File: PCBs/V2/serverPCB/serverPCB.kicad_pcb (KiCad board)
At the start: 2 copper layers, 53.3 x 66 mm, 8 parts, among them J2 Screw_Terminal_01x04, U4 TPSM84203

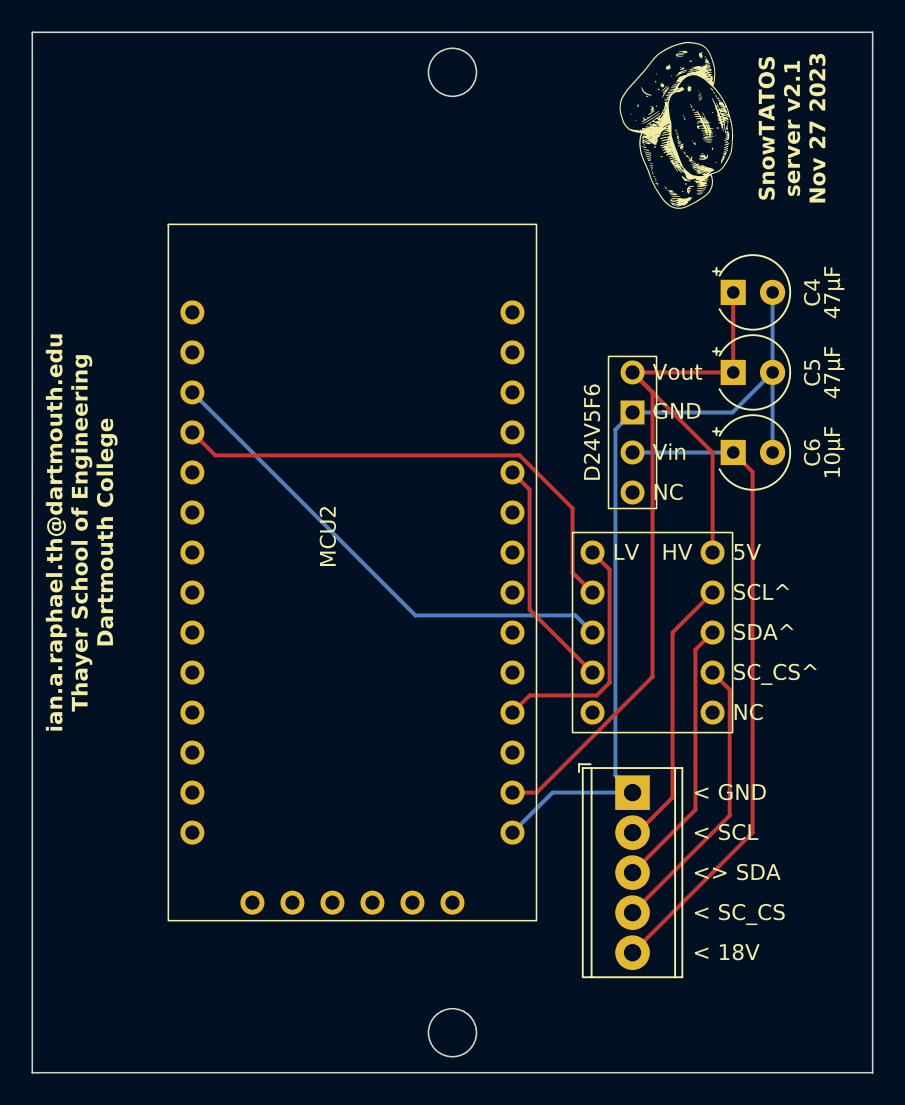
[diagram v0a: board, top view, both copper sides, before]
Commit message: fully updated but untested server/node code for new mini ultra boards
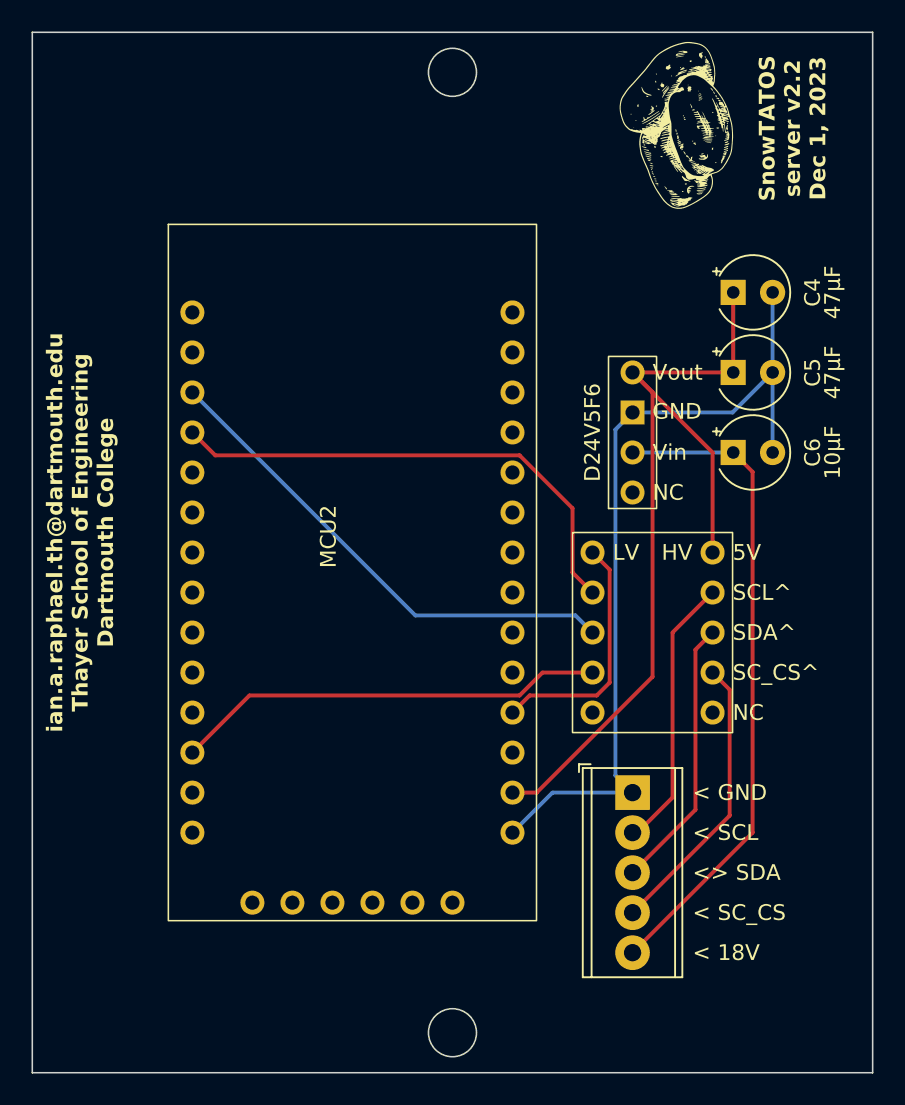
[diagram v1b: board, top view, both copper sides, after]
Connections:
- MCU2 pad 11: unconnected-(MCU2-D11-Pad11) -> /SC_CS
- MCU2 pad A2: Net-(MCU2-A2_D14) -> unconnected-(MCU2-A2_D14-PadA2)
- U3 pad 4: Net-(MCU2-A2_D14) -> /SC_CS
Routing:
- net /SC_CS: track 0.00 -> 27.5 mm
- net Net-(MCU2-A2_D14): track 14.8 -> 0.00 mm
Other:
- board text added: "SnowTATOS server v2.2 Dec 1, 2023"
- board text removed: "SnowTATOS server v2.1 Nov 27 2023"
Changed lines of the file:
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@@
   (net 20 "unconnected-(MCU2-RXD1-Pad9)")
   (net 21 "unconnected-(MCU2-LORA_DIO_0-Pad10)")
-  (net 22 "unconnected-(MCU2-D11-Pad11)")
+  (net 22 "/SC_CS")
   (net 23 "unconnected-(MCU2-LORA_CS-Pad12)")
   (net 24 "unconnected-(MCU2-D13_A1-Pad13)")
@@
   (net 26 "unconnected-(MCU2-D23-Pad23)")
   (net 27 "unconnected-(MCU2-D24-Pad24)")
-  (net 28 "Net-(MCU2-A2_D14)")
+  (net 28 "unconnected-(MCU2-A2_D14-PadA2)")
   (net 29 "unconnected-(MCU2-A3_D15-PadA3)")
   (net 30 "unconnected-(MCU2-A4_D16-PadA4)")
@@
       (net 21 "unconnected-(MCU2-LORA_DIO_0-Pad10)") (pinfunction "LORA_DIO_0") (pintype "bidirectional"))
     (pad "11" thru_hole circle (at -10.16 7.62) (size 1.524 1.524) (drill 0.9) (layers "*.Cu" "*.Mask")
-      (net 22 "unconnected-(MCU2-D11-Pad11)") (pinfunction "D11") (pintype "unspecified"))
+      (net 22 "/SC_CS") (pinfunction "D11") (pintype "unspecified"))
     (pad "12" thru_hole circle (at -10.16 10.16) (size 1.524 1.524) (drill 0.9) (layers "*.Cu" "*.Mask")
       (net 23 "unconnected-(MCU2-LORA_CS-Pad12)") (pinfunction "LORA_CS") (pintype "output"))
@@
       (net 8 "unconnected-(MCU2-D25-Pad25)") (pinfunction "D25") (pintype "bidirectional"))
     (pad "A2" thru_hole circle (at 10.16 -10.16) (size 1.524 1.524) (drill 0.9) (layers "*.Cu" "*.Mask")
-      (net 28 "Net-(MCU2-A2_D14)") (pinfunction "A2_D14") (pintype "bidirectional"))
+      (net 28 "unconnected-(MCU2-A2_D14-PadA2)") (pinfunction "A2_D14") (pintype "bidirectional"))
     (pad "A3" thru_hole circle (at 10.16 -12.7) (size 1.524 1.524) (drill 0.9) (layers "*.Cu" "*.Mask")
       (net 29 "unconnected-(MCU2-A3_D15-PadA3)") (pinfunction "A3_D15") (pintype "bidirectional"))
@@
       (net 7 "/SDA") (pinfunction "L2") (pintype "bidirectional"))
     (pad "4" thru_hole circle (at -3.81 2.54) (size 1.524 1.524) (drill 0.9) (layers "*.Cu" "*.Mask")
-      (net 28 "Net-(MCU2-A2_D14)") (pinfunction "L3") (pintype "bidirectional"))
+      (net 22 "/SC_CS") (pinfunction "L3") (pintype "bidirectional"))
     (pad "5" thru_hole circle (at -3.81 5.08) (size 1.524 1.524) (drill 0.9) (layers "*.Cu" "*.Mask")
       (net 9 "unconnected-(U3-L4-Pad5)") (pinfunction "L4") (pintype "bidirectional+no_connect"))
@@
     (effects (font (size 1 1) (thickness 0.15)) (justify left))
   )
-  (gr_text "SnowTATOS\nserver v2.1\nNov 27 2023" (at 162.56 64.516 90) (layer "F.SilkS")
+  (gr_text "SnowTATOS\nserver v2.2\nDec 1, 2023" (at 162.56 64.516 90) (layer "F.SilkS")
     (effects (font (size 1 1) (thickness 0.2) bold))
   )
@@
   (segment (start 158.79 74.93) (end 158.79 80.01) (width 0.25) (layer "F.Cu") (net 10))
   (segment (start 152.4 80.01) (end 157.48 85.09) (width 0.25) (layer "F.Cu") (net 10))
-  (segment (start 145.867 87.447) (end 145.867 95.067) (width 0.25) (layer "F.Cu") (net 28))
-  (segment (start 145.867 95.067) (end 149.86 99.06) (width 0.25) (layer "F.Cu") (net 28))
-  (segment (start 144.78 86.36) (end 145.867 87.447) (width 0.25) (layer "F.Cu") (net 28))
+  (segment (start 128.086823 100.513177) (end 124.46 104.14) (width 0.25) (layer "F.Cu") (net 22))
+  (segment (start 145.230427 100.513177) (end 128.086823 100.513177) (width 0.25) (layer "F.Cu") (net 22))
+  (segment (start 146.683604 99.06) (end 145.230427 100.513177) (width 0.25) (layer "F.Cu") (net 22))
+  (segment (start 149.86 99.06) (end 146.683604 99.06) (width 0.25) (layer "F.Cu") (net 22))
   (segment (start 160.02 109.22) (end 160.02 86.32) (width 0.25) (layer "F.Cu") (net 39))
   (segment (start 160.02 86.32) (end 158.79 85.09) (width 0.25) (layer "F.Cu") (net 39))

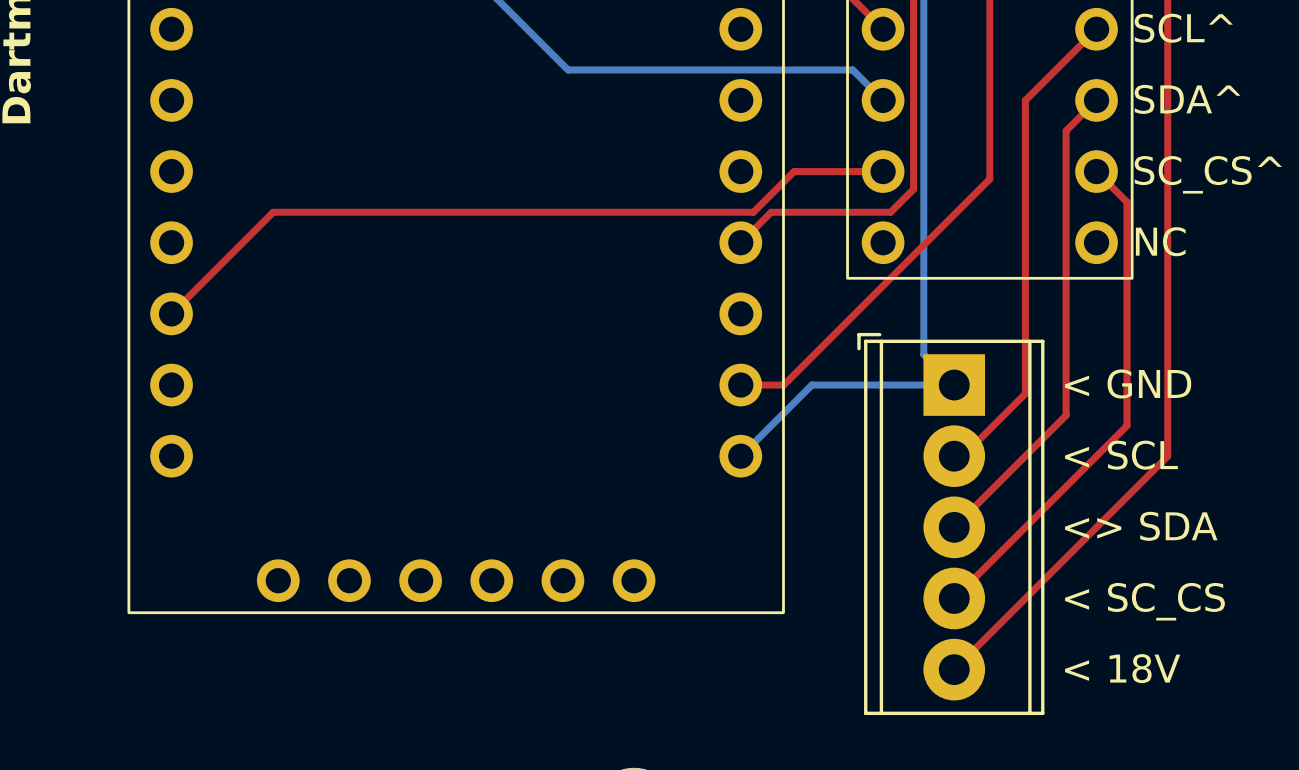
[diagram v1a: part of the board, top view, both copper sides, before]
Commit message: successful server integration into barebones simb program and full simb suite with dummy buffer
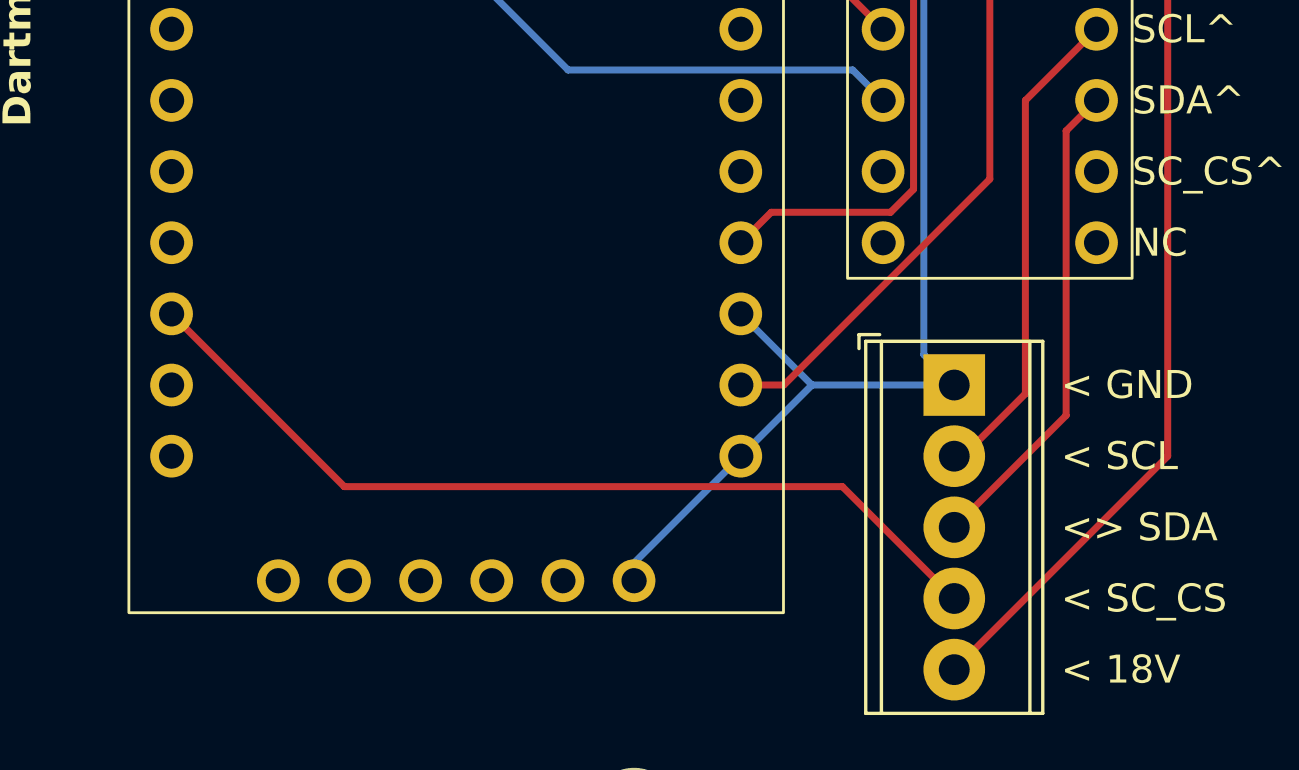
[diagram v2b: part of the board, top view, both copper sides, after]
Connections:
- J2 pad 4: Net-(J2-Pin_4) -> /SC_CS
- U3 pad 4: /SC_CS -> unconnected-(U3-L3-Pad4)
- U3 pad 9: Net-(J2-Pin_4) -> unconnected-(U3-H3-Pad9)
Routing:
- net Net-(J2-Pin_4): track 18.2 -> 0.00 mm
- net /GND: track 53.8 -> 63.4 mm
- net /SC_CS: track 27.5 -> 32.1 mm
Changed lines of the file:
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@@
   (net 2 "Net-(J2-Pin_2)")
   (net 3 "Net-(J2-Pin_3)")
-  (net 4 "Net-(J2-Pin_4)")
+  (net 4 "unconnected-(U3-L3-Pad4)")
   (net 5 "/3v3")
   (net 6 "/SCL")
@@
   (net 38 "unconnected-(MCU2-PadVIN)")
   (net 39 "Net-(J2-Pin_5)")
+  (net 40 "unconnected-(U3-H3-Pad9)")
   (footprint "Capacitor_THT:CP_Radial_Tantal_D4.5mm_P2.50mm" (layer "F.Cu")
     (at 158.79 85.09)
@@
       (net 3 "Net-(J2-Pin_3)") (pinfunction "Pin_3") (pintype "passive"))
     (pad "4" thru_hole circle (at 7.62 0 270) (size 2.2 2.2) (drill 1.1) (layers "*.Cu" "*.Mask")
-      (net 4 "Net-(J2-Pin_4)") (pinfunction "Pin_4") (pintype "passive"))
+      (net 22 "/SC_CS") (pinfunction "Pin_4") (pintype "passive"))
     (pad "5" thru_hole circle (at 10.16 0 270) (size 2.2 2.2) (drill 1.1) (layers "*.Cu" "*.Mask")
       (net 39 "Net-(J2-Pin_5)") (pinfunction "Pin_5") (pintype "passive"))
@@
       (net 7 "/SDA") (pinfunction "L2") (pintype "bidirectional"))
     (pad "4" thru_hole circle (at -3.81 2.54) (size 1.524 1.524) (drill 0.9) (layers "*.Cu" "*.Mask")
-      (net 22 "/SC_CS") (pinfunction "L3") (pintype "bidirectional"))
+      (net 4 "unconnected-(U3-L3-Pad4)") (pinfunction "L3") (pintype "bidirectional"))
     (pad "5" thru_hole circle (at -3.81 5.08) (size 1.524 1.524) (drill 0.9) (layers "*.Cu" "*.Mask")
       (net 9 "unconnected-(U3-L4-Pad5)") (pinfunction "L4") (pintype "bidirectional+no_connect"))
@@
       (net 3 "Net-(J2-Pin_3)") (pinfunction "H2") (pintype "bidirectional"))
     (pad "9" thru_hole circle (at 3.81 2.54) (size 1.524 1.524) (drill 0.9) (layers "*.Cu" "*.Mask")
-      (net 4 "Net-(J2-Pin_4)") (pinfunction "H3") (pintype "bidirectional"))
+      (net 40 "unconnected-(U3-H3-Pad9)") (pinfunction "H3") (pintype "bidirectional"))
     (pad "10" thru_hole circle (at 3.81 5.08) (size 1.524 1.524) (drill 0.9) (layers "*.Cu" "*.Mask")
       (net 11 "unconnected-(U3-H4-Pad10)") (pinfunction "H4") (pintype "bidirectional+no_connect"))
@@
   (segment (start 161.29 80.01) (end 158.75 82.55) (width 0.25) (layer "B.Cu") (net 1))
   (segment (start 152.4 106.68) (end 147.32 106.68) (width 0.25) (layer "B.Cu") (net 1))
+  (segment (start 144.78 109.22) (end 140.97 113.03) (width 0.25) (layer "B.Cu") (net 1))
   (segment (start 158.75 82.55) (end 152.4 82.55) (width 0.25) (layer "B.Cu") (net 1))
   (segment (start 161.29 74.93) (end 161.29 85.09) (width 0.25) (layer "B.Cu") (net 1))
+  (segment (start 140.97 113.03) (end 140.97 113.665) (width 0.25) (layer "B.Cu") (net 1))
   (segment (start 151.313 83.637) (end 151.313 105.593) (width 0.25) (layer "B.Cu") (net 1))
   (segment (start 152.4 82.55) (end 151.313 83.637) (width 0.25) (layer "B.Cu") (net 1))
+  (segment (start 147.32 106.68) (end 144.78 104.14) (width 0.25) (layer "B.Cu") (net 1))
   (segment (start 151.313 105.593) (end 152.4 106.68) (width 0.25) (layer "B.Cu") (net 1))
   (segment (start 152.71 109.22) (end 154.94 106.99) (width 0.25) (layer "F.Cu") (net 2))
@@
   (segment (start 156.393 107.767) (end 156.393 97.607) (width 0.25) (layer "F.Cu") (net 3))
   (segment (start 156.393 97.607) (end 157.48 96.52) (width 0.25) (layer "F.Cu") (net 3))
-  (segment (start 152.4 114.3) (end 158.567 108.133) (width 0.25) (layer "F.Cu") (net 4))
-  (segment (start 158.567 108.133) (end 158.567 100.147) (width 0.25) (layer "F.Cu") (net 4))
-  (segment (start 158.567 100.147) (end 157.48 99.06) (width 0.25) (layer "F.Cu") (net 4))
   (segment (start 150.947 99.693251) (end 150.127251 100.513) (width 0.25) (layer "F.Cu") (net 5))
   (segment (start 145.867 100.513) (end 144.78 101.6) (width 0.25) (layer "F.Cu") (net 5))
@@
   (segment (start 158.79 74.93) (end 158.79 80.01) (width 0.25) (layer "F.Cu") (net 10))
   (segment (start 152.4 80.01) (end 157.48 85.09) (width 0.25) (layer "F.Cu") (net 10))
-  (segment (start 128.086823 100.513177) (end 124.46 104.14) (width 0.25) (layer "F.Cu") (net 22))
-  (segment (start 145.230427 100.513177) (end 128.086823 100.513177) (width 0.25) (layer "F.Cu") (net 22))
-  (segment (start 146.683604 99.06) (end 145.230427 100.513177) (width 0.25) (layer "F.Cu") (net 22))
-  (segment (start 149.86 99.06) (end 146.683604 99.06) (width 0.25) (layer "F.Cu") (net 22))
+  (segment (start 124.46 104.14) (end 130.627 110.307) (width 0.25) (layer "F.Cu") (net 22))
+  (segment (start 148.407 110.307) (end 152.4 114.3) (width 0.25) (layer "F.Cu") (net 22))
+  (segment (start 130.627 110.307) (end 148.407 110.307) (width 0.25) (layer "F.Cu") (net 22))
   (segment (start 160.02 109.22) (end 160.02 86.32) (width 0.25) (layer "F.Cu") (net 39))
   (segment (start 160.02 86.32) (end 158.79 85.09) (width 0.25) (layer "F.Cu") (net 39))

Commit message: fixed pinger read error
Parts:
- removed U3: ~, Converter_DCDC:Pololu_logicLevelShifter
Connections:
- J2 pad 2: Net-(J2-Pin_2) -> /SDA
- J2 pad 3: Net-(J2-Pin_3) -> /SCL
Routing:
- net Net-(J2-Pin_2): track 17.5 -> 0.00 mm
- net Net-(J2-Pin_3): track 17.3 -> 0.00 mm
- net /3v3: track 15.7 -> 0.00 mm
- net /VBAT: track 56.8 -> 43.2 mm
- net /SDA: track 31.7 -> 43.4 mm
- net /SCL: track 32.0 -> 43.4 mm
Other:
- board text added: "SnowTATOS server v2.3 Jan 9, 2024"
- board text removed: "5V"
- board text removed: "HV"
- board text removed: "LV"
- board text removed: "SCL^"
- board text removed: "SC_CS^"
- board text removed: "SDA^"
- board text removed: "SnowTATOS server v2.2 Dec 1, 2023"
